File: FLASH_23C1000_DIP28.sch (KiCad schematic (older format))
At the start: 8 parts, among them J1 uPD23C1000, J2 Conn_1x2, J3 Conn_1x3, U1 29F010 TSOP-32 20mm, U2 29F010 sTSOP-32 14mm, U3 29F010 PLCC-32 7x9

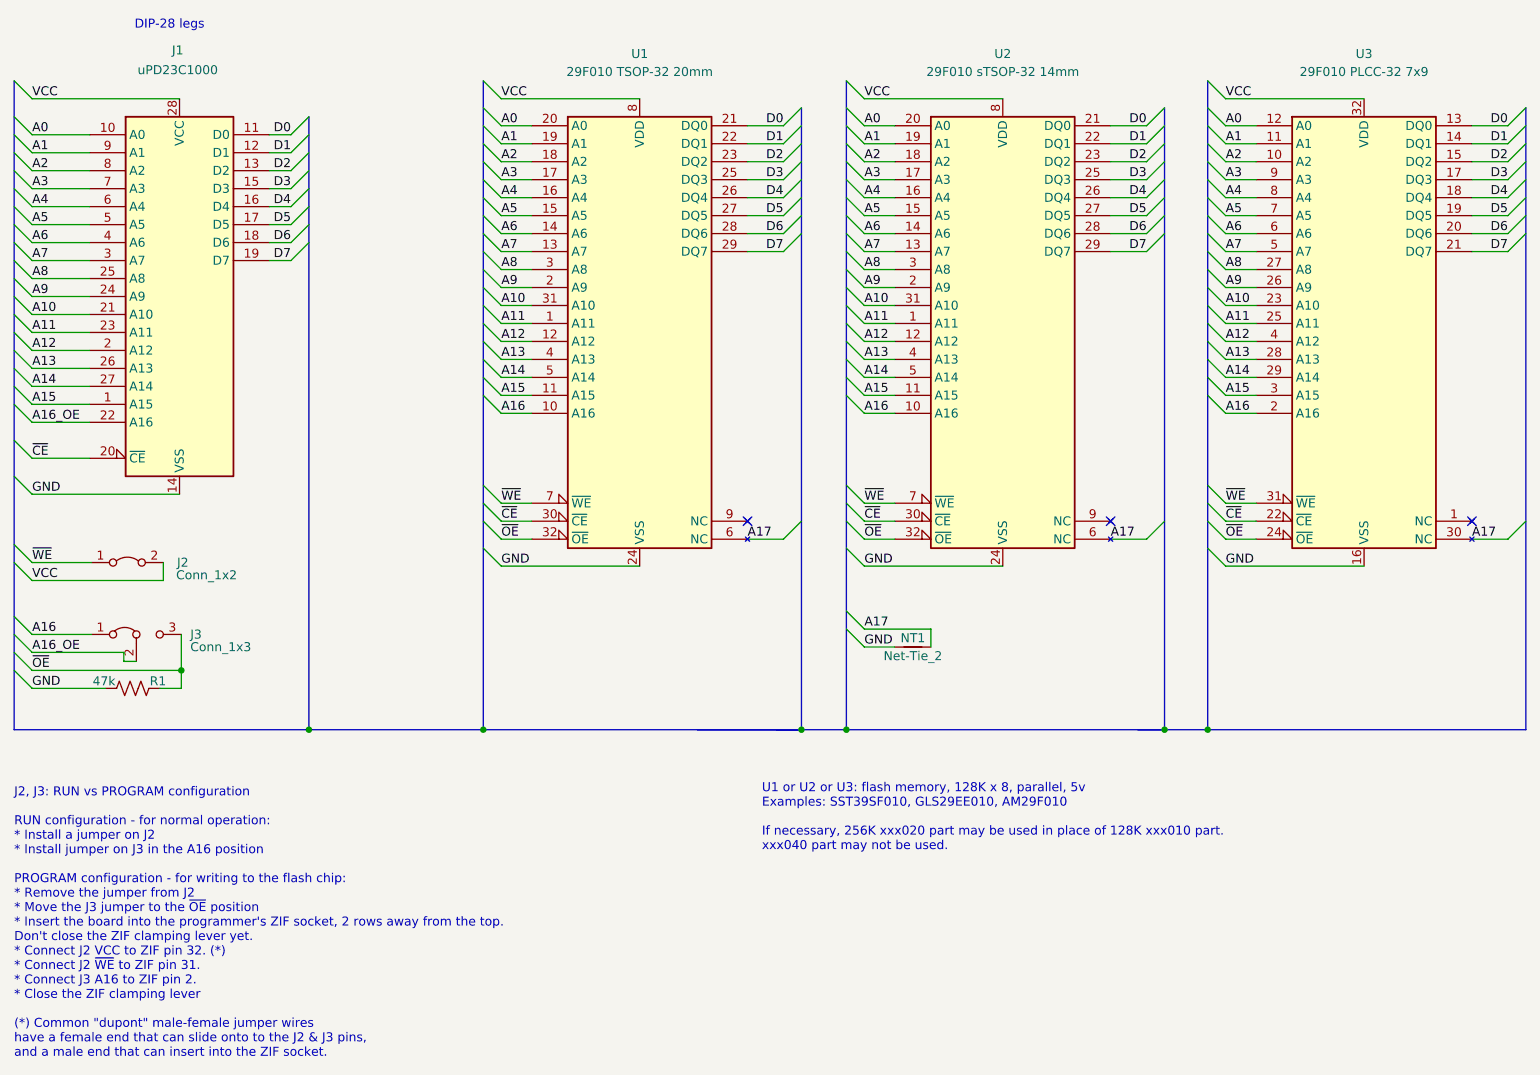
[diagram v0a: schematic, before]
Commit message: Rename FlashROM_8300 to FLASH_23C1000
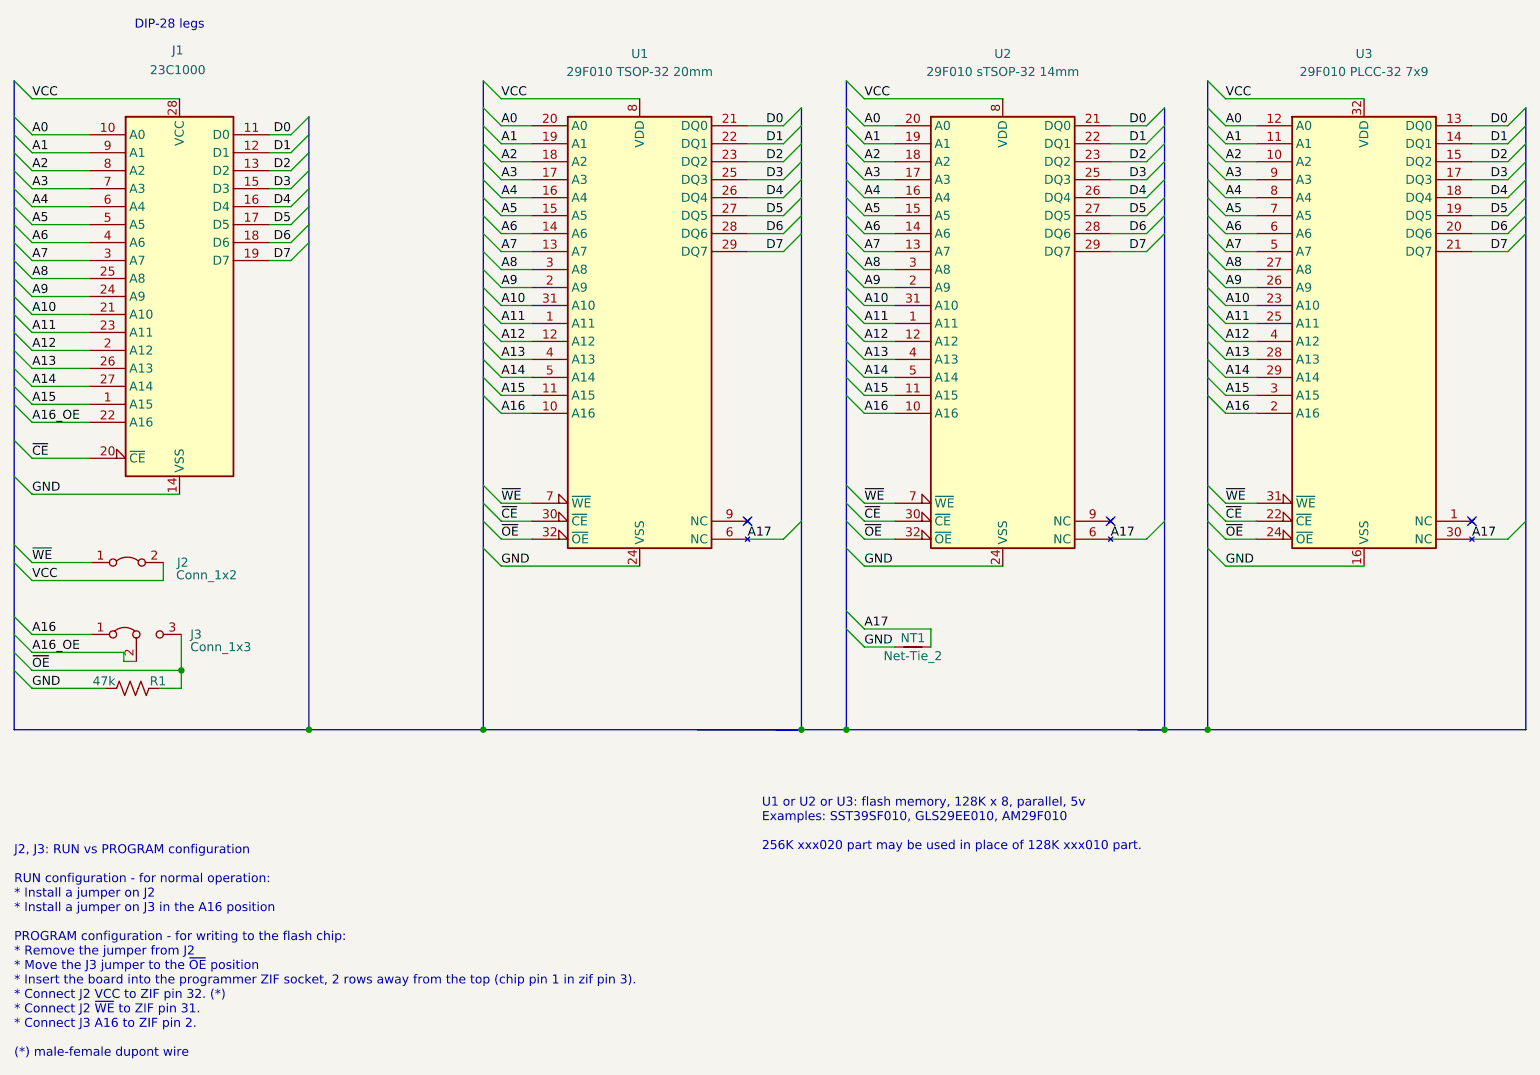
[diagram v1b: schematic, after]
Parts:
- J1: value uPD23C1000 -> 23C1000
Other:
- note added: "J2, J3: RUN vs PROGRAM configuration\n\nRUN configuration - for normal operation:\n* Install a jumper on J2\n* Install a jumper on J3 in the A16 position\n\nPROGRAM configuration - for writing to the flash chip:\n* Remove the jumper from J2\n* Move the J3 jumper to the ~OE~ position\n* Insert the board into the programmer ZIF socket, 2 rows away from the top (chip pin 1 in zif pin 3).\n* Connect 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"
- note added: "U1 or U2 or U3: flash memory, 128K x 8, parallel, 5v\nExamples: SST39SF010, GLS29EE010, AM29F010\n\n256K xxx020 part may be used in place of 128K xxx010 part.\n"
- note removed: "J2, J3: RUN vs PROGRAM configuration\n\nRUN configuration - for normal operation:\n* Install a jumper on J2\n* Install jumper on J3 in the A16 position\n\nPROGRAM configuration - for writing to the flash chip:\n* Remove the jumper from J2\n* Move the J3 jumper to the ~OE~ position\n* Insert the board into the programmer's ZIF socket, 2 rows away from the top.\nDon't close the ZIF clamping lever y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"
- note removed: "U1 or U2 or U3: flash memory, 128K x 8, parallel, 5v\nExamples: SST39SF010, GLS29EE010, AM29F010\n\nIf necessary, 256K xxx020 part may be used in place of 128K xxx010 part.\nxxx040 part may not be used.\n"
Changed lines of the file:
@@
 encoding utf-8
 Sheet 1 1
-Title "29F010 to uPD23C1000"
-Date "2020-11-23"
-Rev "002"
+Title "29F010 to 23C1000"
+Date "2021-05-09"
+Rev "003"
 Comp "Brian K. White - b.kenyon.w@gmail.com"
 Comment1 ""
@@
 P 2120 2600
 F 0 "J1" H 2110 3970 50  0000 C CNN
-F 1 "uPD23C1000" H 2110 3860 50  0000 C CNN
+F 1 "23C1000" H 2110 3860 50  0000 C CNN
 F 2 "000_LOCAL:DIP28_0.6_pcb_sil_pins" H 2120 2600 50  0001 C CNN
 F 3 "http://ww1.microchip.com/downloads/en/DeviceDoc/doc0014.pdf" H 2120 2600 50  0001 C CNN
@@
 DIP-28 legs
 Text Notes 1200 6840 0    50   ~ 0
-J2, J3: RUN vs PROGRAM configuration\n\nRUN configuration - for normal operation:\n* Install a jumper on J2\n* Install jumper on J3 in the A16 position\n\nPROGRAM configuration - for writing to the flash chip:\n* Remove the jumper from J2\n* Move the J3 jumper to the ~OE~ position\n* Insert the board into the programmer's ZIF socket, 2 rows away from the top.\nDon't close the ZIF clamping lever yet.\n* Connect J2 VCC to ZIF pin 32. (*)\n* Connect J2 ~WE~ to ZIF pin 31.\n* Connect J3 A16 to ZIF pin 2.\n* Close the ZIF clamping lever\n\n(*) Common "dupont" male-female jumper wires\nhave a female end that can slide onto to the J2 & J3 pins,\nand a male end that can insert into the ZIF socket.\n
+J2, J3: RUN vs PROGRAM configuration\n\nRUN configuration - for normal operation:\n* Install a jumper on J2\n* Install a jumper on J3 in the A16 position\n\nPROGRAM configuration - for writing to the flash chip:\n* Remove the jumper from J2\n* Move the J3 jumper to the ~OE~ position\n* Insert the board into the programmer ZIF socket, 2 rows away from the top (chip pin 1 in zif pin 3).\n* Connect J2 VCC to ZIF pin 32. (*)\n* Connect J2 ~WE~ to ZIF pin 31.\n* Connect J3 A16 to ZIF pin 2.\n\n(*) male-female dupont wire\n
 Text Label 5280 3950 0    50   ~ 0
 A17
@@
 NoConn ~ 5280 3850
 Text Notes 5360 5690 0    50   ~ 0
-U1 or U2 or U3: flash memory, 128K x 8, parallel, 5v\nExamples: SST39SF010, GLS29EE010, AM29F010\n\nIf necessary, 256K xxx020 part may be used in place of 128K xxx010 part.\nxxx040 part may not be used.\n
+U1 or U2 or U3: flash memory, 128K x 8, parallel, 5v\nExamples: SST39SF010, GLS29EE010, AM29F010\n\n256K xxx020 part may be used in place of 128K xxx010 part.\n
 $Comp
 L 000_LOCAL:Net-Tie_2 NT1
